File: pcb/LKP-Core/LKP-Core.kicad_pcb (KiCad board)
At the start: 2 copper layers, 41 x 34 mm, 29 parts, among them J1 Intercon L, J2 Intercon R, J3 Power JST PH, J4 IO, J5 SWD, J6 WS281x, U1 CY8C4246AZI-M445

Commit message: Misc
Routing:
- net GND: vias 51 -> 50
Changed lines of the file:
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@@
     (thickness 1.6)
     (drawings 7)
-    (tracks 486)
+    (tracks 485)
     (zones 0)
     (modules 29)
@@
     (46 B.CrtYd user)
     (47 F.CrtYd user)
-    (48 B.Fab user)
-    (49 F.Fab user)
+    (48 B.Fab user hide)
+    (49 F.Fab user hide)
   )
   (setup
@@
   (via (at 149.275 94.6) (size 0.8) (drill 0.4) (layers F.Cu B.Cu) (net 1))
   (via (at 149.975 100.8) (size 0.8) (drill 0.4) (layers F.Cu B.Cu) (net 1))
-  (via (at 146.075 90.8) (size 0.8) (drill 0.4) (layers F.Cu B.Cu) (net 1))
   (segment (start 142.431847 90.243153) (end 143.531847 91.343153) (width 0.5) (layer B.Cu) (net 1) (status 30))
   (segment (start 154.631847 104.293153) (end 154.606847 104.268153) (width 0.5) (layer B.Cu) (net 1) (status 30))
@@
   (via (at 150.375 87.8) (size 0.8) (drill 0.4) (layers F.Cu B.Cu) (net 1))
   (via (at 141.875 87.4) (size 0.8) (drill 0.4) (layers F.Cu B.Cu) (net 1))
-  (via (at 144.075 89.4) (size 0.8) (drill 0.4) (layers F.Cu B.Cu) (net 1))
+  (via (at 144.475 90.4) (size 0.8) (drill 0.4) (layers F.Cu B.Cu) (net 1))
   (via (at 155.075 97.8) (size 0.8) (drill 0.4) (layers F.Cu B.Cu) (net 1))
   (via (at 140.275 98) (size 0.8) (drill 0.4) (layers F.Cu B.Cu) (net 1))
@@
       )
     )
+  )
+  (zone (net 0) (net_name "") (layer F.Cu) (hatch edge 0.508)
+    (connect_pads (clearance 0.2))
+    (min_thickness 0.254)
+    (keepout (tracks allowed) (vias allowed) (copperpour not_allowed))
+    (fill (arc_segments 32) (thermal_gap 0.508) (thermal_bridge_width 0.508))
+    (polygon
+      (pts
+        (xy 157.875 86.2) (xy 166.875 86.2) (xy 166.875 109) (xy 157.875 109)
+      )
+    )

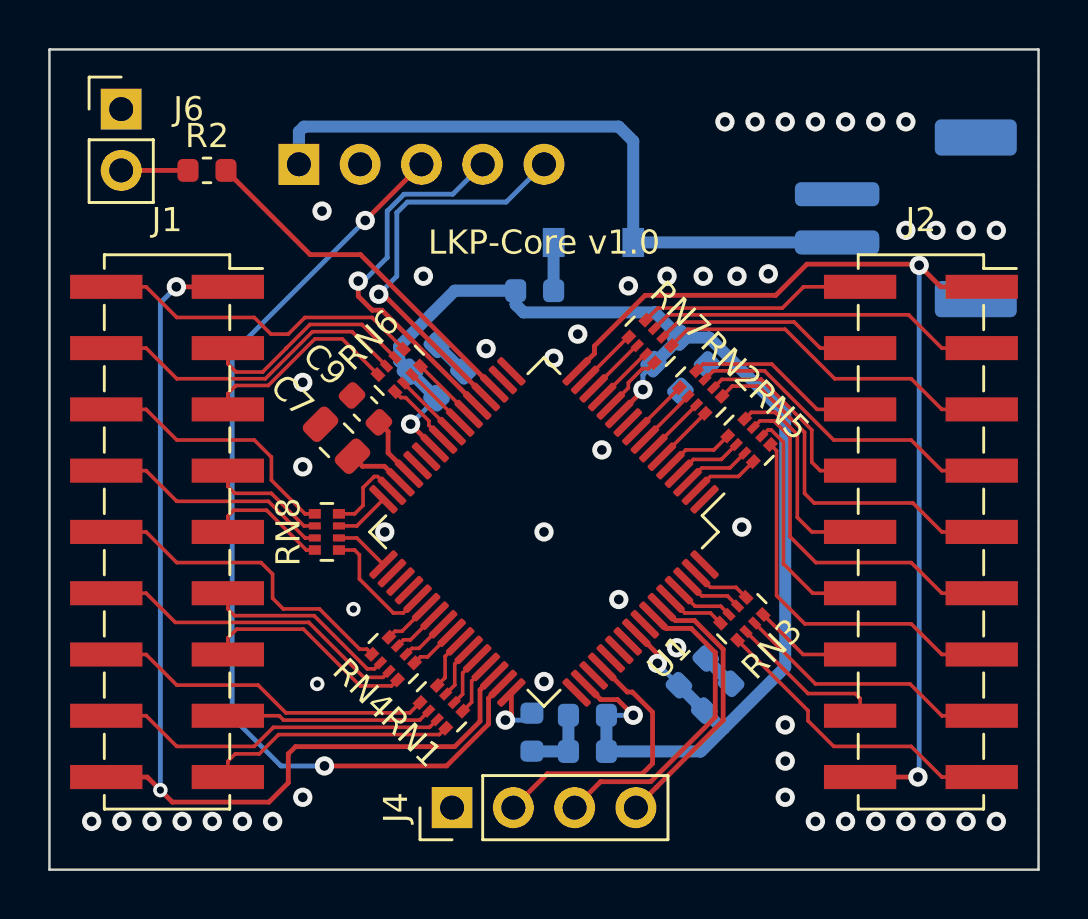
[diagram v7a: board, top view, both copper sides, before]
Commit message: Refactor right side routing
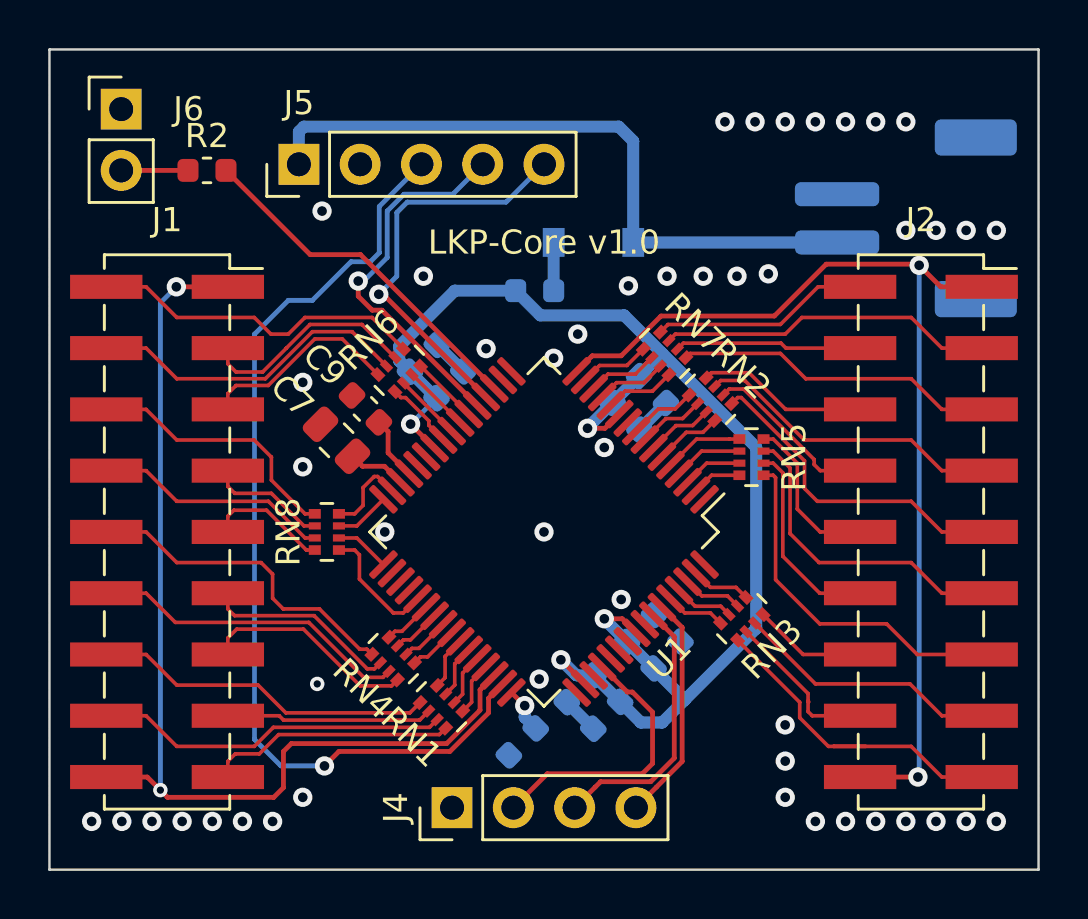
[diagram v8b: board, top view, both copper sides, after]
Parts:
- J5: moved to F.Cu
- moved C6 2.80 mm to (150.9, 102.0)
- moved C8 2.73 mm to (152.0, 103.1)
- moved C4 2.33 mm to (150.3, 93.2)
- moved C5 2.33 mm to (151.4, 92.1)
- moved C3 1.70 mm to (149.5, 105.6), turned to 225 degrees
- moved C1 1.14 mm to (148.4, 104.5), turned to 225 degrees
- moved RN7 0.78 mm to (151.9, 90.6)
- moved RN5 0.71 mm to (155.5, 94.9), turned to 180 degrees
- moved C2 0.57 mm to (146.0, 106.7), turned to 225 degrees
- moved RN2 0.50 mm to (153.8, 92.5)
- turned J5 to 90 degrees
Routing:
- net VDD: track 59.4 -> 56.2 mm
- net /E1_6: track 15.4 -> 13.1 mm
- net /E1_7: track 8.96 -> 6.71 mm
- net /I2C_SCL: track 13.3 -> 11.2 mm
- net /I2C_SDA: track 11.3 -> 9.45 mm
- net /E1_5: track 9.94 -> 8.27 mm
- net /E1_8: track 14.9 -> 13.4 mm
- net /E1_0: track 12.7 -> 14.2 mm
- net GND: track 6.06 -> 4.67 mm, vias 50 -> 47
- net /E1_9: track 8.65 -> 7.30 mm
- net /E1_4: track 15.9 -> 14.6 mm
- net /E1_12: track 14.5 -> 13.3 mm
- net /E1_13: track 8.88 -> 7.76 mm
- net /S1_4: track 2.88 -> 2.06 mm
- net /E1_10: track 13.3 -> 12.7 mm
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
